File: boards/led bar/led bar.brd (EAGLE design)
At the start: 130 x 85 mm, 7 parts

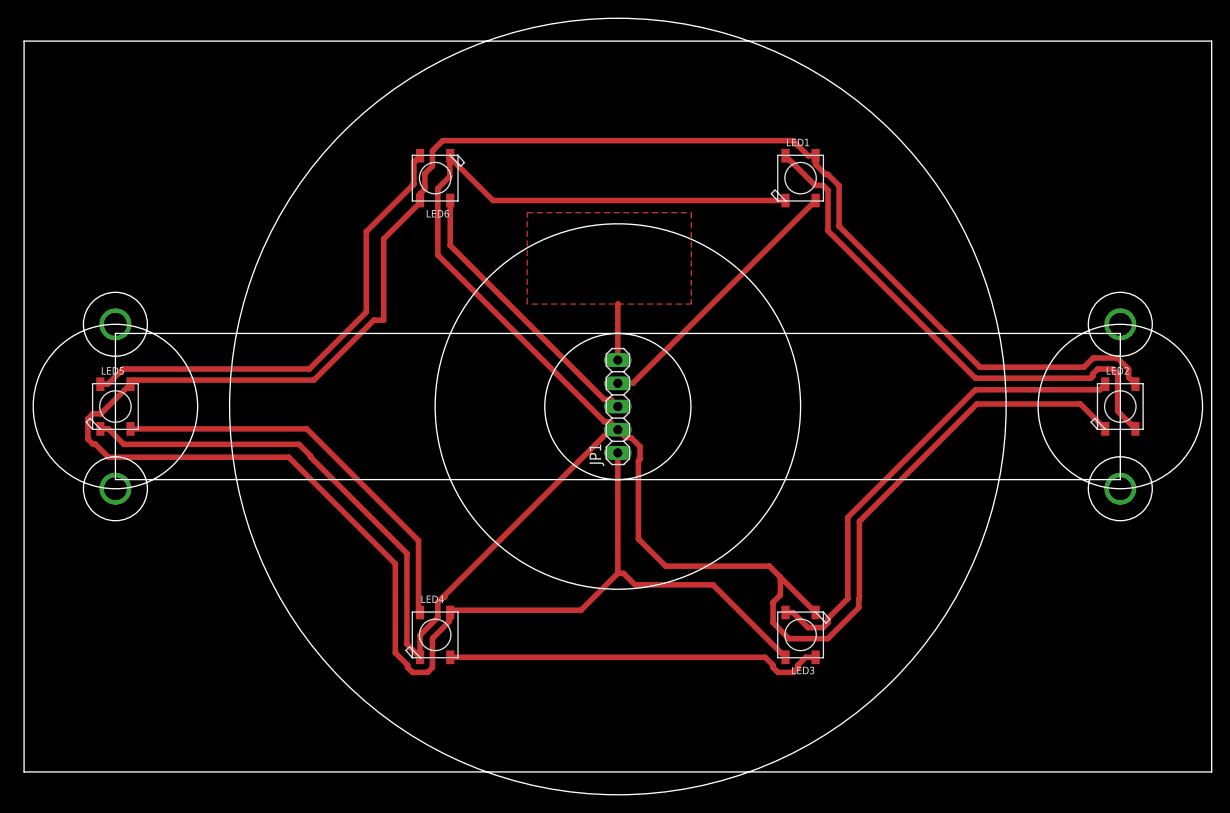
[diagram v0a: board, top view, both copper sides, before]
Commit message: added led bar circuit board
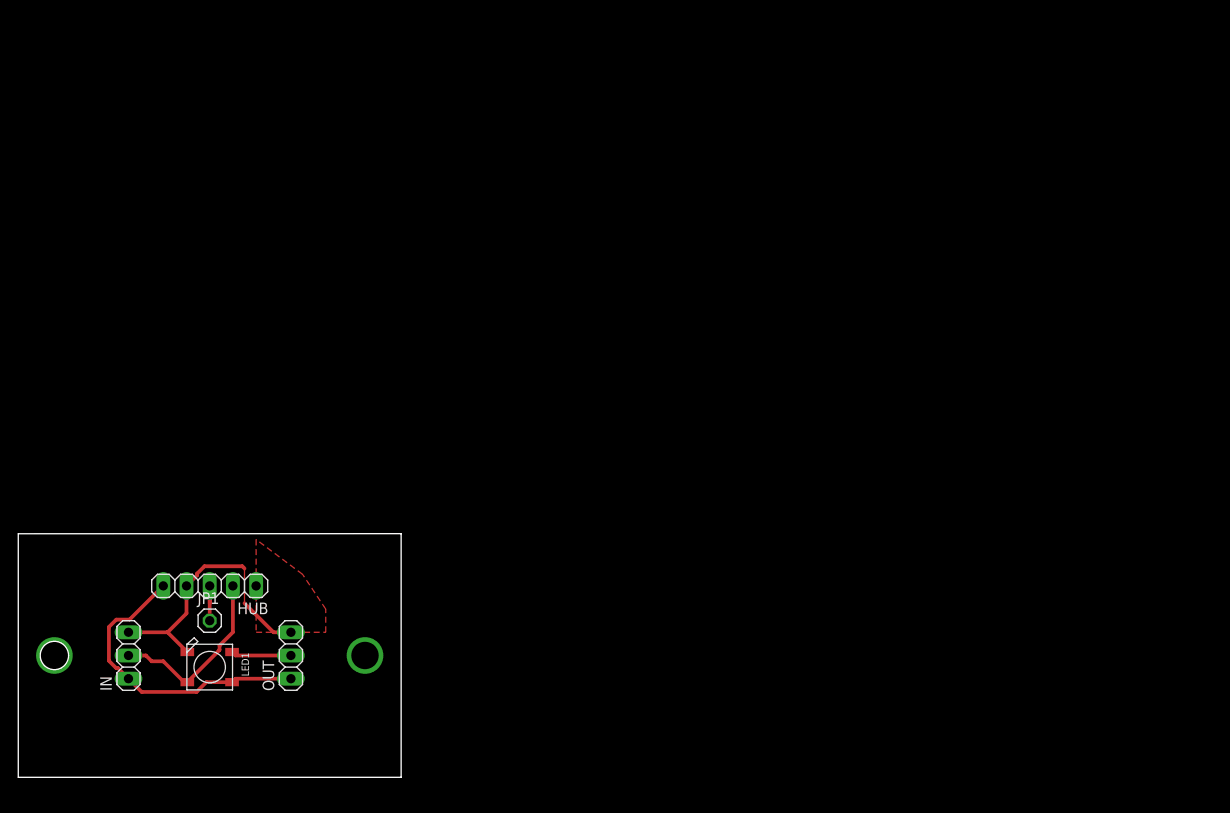
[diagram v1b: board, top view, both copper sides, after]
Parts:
- removed LED2, LED3, LED4, LED5, LED6: WS2812B5050, adafruit:WS2812B
- added HUB: (no value), pinhead:1X05
- added IN, OUT: (no value), pinhead:1X03
- JP1: device pinhead:1X05 -> pinhead:1X01
- moved LED1 84.0 mm to (20.3, 11.4), turned to 0 degrees
- moved JP1 50.5 mm to (20.3, 16.5), turned to 0 degrees
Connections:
- removed net N$10: LED5.2-DOUT, LED6.4-DIN
- removed net N$3: JP1.4, LED1.4-DIN
- removed net N$4: JP1.3, LED6.2-DOUT
- removed net N$6: LED1.2-DOUT, LED2.4-DIN
- removed net N$7: LED2.2-DOUT, LED3.4-DIN
- removed net N$8: LED3.2-DOUT, LED4.4-DIN
- removed net N$9: LED4.2-DOUT, LED5.4-DIN
- removed net VDD: JP1.1, LED1.1-VDD, LED2.1-VDD, LED3.1-VDD, LED4.1-VDD, LED5.1-VDD, LED6.1-VDD
- new net 5V: HUB.5, IN.1, LED1.1-VDD, OUT.1
- new net DATAIN1: HUB.2, IN.2, LED1.4-DIN
- new net DATAOUT1: HUB.3, JP1.1
- new net DATAOUT2: LED1.2-DOUT, OUT.2
- net CAP: now also HUB.1; no longer JP1.5
- net GND: now also HUB.4, IN.3, OUT.3; no longer JP1.2, LED2.3-GND, LED3.3-GND, LED4.3-GND, LED5.3-GND, LED6.3-GND
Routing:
- net VDD: track 270.4 -> 0.00 mm
- net GND: track 259.8 -> 30.9 mm
- net N$6: track 56.7 -> 0.00 mm
- net N$7: track 52.2 -> 0.00 mm
- net N$10: track 52.0 -> 0.00 mm
- net N$9: track 44.5 -> 0.00 mm
- net N$8: track 41.7 -> 0.00 mm
- net 5V: track 0.00 -> 33.7 mm
- net N$4: track 30.6 -> 0.00 mm
- net N$3: track 29.9 -> 0.00 mm
- net DATAIN1: track 0.00 -> 20.3 mm
- net DATAOUT2: track 0.00 -> 6.60 mm
- net CAP: track 6.16 -> 0.00 mm
- net DATAOUT1: track 0.00 -> 5.71 mm
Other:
- board size 130 x 85 mm -> 41.9 x 26.7 mm
